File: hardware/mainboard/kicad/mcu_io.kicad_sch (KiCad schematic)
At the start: 37 parts, among them J2 Hirose DM3AT-SF-PEJM5, SW2 BOOT / RECOVERY, SW3 TL3340AF160QG, SW4 TL3340AF160QG, SW5 TL3340AF160QG, SW6 TL3340AF160QG, U1 ESP32-S3-WROOM-1-N16R8, U10 TLV3012BIDBVR, U5 BMI270, U9 TMUX1101DBVR

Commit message: R129: fix IC stencil apertures, pin-1 marking and native assembly classification
Verify six active IC pin maps and 97 native CPL placements. Preserve all 425 original pads, nets and 2639 tracks/vias; retain the 20 active intrinsic hole-clearance findings as fabrication gates. Add independent native KiCad checks and exact source-preservation guards.
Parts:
- U10: Assembly (none) -> FIT; MPN (none) -> TLV3012BIDBVR; Manufacturer (none) -> Texas Instruments
- U5: Assembly (none) -> FIT; MPN (none) -> BMI270; Manufacturer (none) -> Bosch Sensortec
- U9: Assembly (none) -> FIT; MPN (none) -> TMUX1101DBVR; Manufacturer (none) -> Texas Instruments
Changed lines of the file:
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@@
 		(property "Value" "BMI270" (at 188.26 132.86 0) (effects (font (size 0.88 0.88))))
 		(property "Footprint" "ENKU:BMI270_Bosch_LGA14" (at 175.26 149.86 0) (effects (font (size 0.88 0.88)) (hide yes)))
-		(property "Datasheet" "~" (at 175.26 149.86 0) (effects (font (size 0.88 0.88)) (hide yes)))
+		(property "Datasheet" "https://www.bosch-sensortec.com/media/boschsensortec/downloads/datasheets/bst-bmi270-ds000.pdf" (at 175.26 149.86 0) (effects (font (size 0.88 0.88)) (hide yes)))
 		(property "Description" "BMI270" (at 175.26 149.86 0) (effects (font (size 0.88 0.88)) (hide yes)))
 		(pin "1")
@@
 		(pin "14")
 		(instances (project "enku-mainboard-r0.1" (path "/10000000-0000-4000-8000-000000000001/74000000-0000-4000-8000-000000000182" (reference "U5") (unit 1))))
+		(property "Manufacturer" "Bosch Sensortec" (at 0 0 0) (effects (font (size .8 .8)) (hide yes)))
+		(property "MPN" "BMI270" (at 0 0 0) (effects (font (size .8 .8)) (hide yes)))
+		(property "Assembly" "FIT" (at 0 0 0) (effects (font (size .8 .8)) (hide yes)))
 	)
 	(global_label "GND" (shape input) (at 160.02 142.24 0) (effects (font (size 0.88 0.88)) (justify right bottom)))
@@
 (pin "5")
 (instances (project "enku-mainboard-r0.1" (path "/10000000-0000-4000-8000-000000000001/e4100000-0000-4000-8000-000000000001" (reference "U9") (unit 1))))
-)
+		(property "Manufacturer" "Texas Instruments" (at 0 0 0) (effects (font (size .8 .8)) (hide yes)))
+		(property "MPN" "TMUX1101DBVR" (at 0 0 0) (effects (font (size .8 .8)) (hide yes)))
+		(property "Assembly" "FIT" (at 0 0 0) (effects (font (size .8 .8)) (hide yes)))
+	)
 	(symbol (lib_id "ENKU:C") (at 367.03 167.64 0) (unit 1) (exclude_from_sim no) (in_bom yes) (on_board yes) (dnp no)
 (property "Reference" "C37" (at 362.03 151.64 0) (effects (font (size 0.88 0.88))))
@@
 (property "Value" "TLV3012BIDBVR" (at 330.2 210.82 0) (effects (font (size 0.88 0.88))))
 (property "Footprint" "ENKU:TLV3012B_DBV0006A" (at 330.2 210.82 0) (effects (font (size 0.88 0.88)) (hide yes)))
-(property "Datasheet" "https://www.ti.com/lit/gpn/TLV3012B" (at 330.2 210.82 0) (effects (font (size 0.88 0.88)) (hide yes)))
+(property "Datasheet" "https://www.ti.com/lit/ds/symlink/tlv3012b.pdf" (at 330.2 210.82 0) (effects (font (size 0.88 0.88)) (hide yes)))
 (property "Description" "TLV3012BIDBVR" (at 330.2 210.82 0) (effects (font (size 0.88 0.88)) (hide yes)))
 (pin "1")
@@
 (pin "5")
 (pin "6")
-(instances (project "enku-mainboard-r0.1" (path "/10000000-0000-4000-8000-000000000001/769db365-4ac6-4285-9803-94ba4cec03fc" (reference "U10") (unit 1)))))
+(instances (project "enku-mainboard-r0.1" (path "/10000000-0000-4000-8000-000000000001/769db365-4ac6-4285-9803-94ba4cec03fc" (reference "U10") (unit 1))))
+		(property "Manufacturer" "Texas Instruments" (at 0 0 0) (effects (font (size .8 .8)) (hide yes)))
+		(property "MPN" "TLV3012BIDBVR" (at 0 0 0) (effects (font (size .8 .8)) (hide yes)))
+		(property "Assembly" "FIT" (at 0 0 0) (effects (font (size .8 .8)) (hide yes)))
+	)
 (global_label "USB_VBUS_VALID" (shape input) (at 340.36 205.74 180) (effects (font (size 0.88 0.88)) (justify right bottom)))
 (global_label "GND" (shape input) (at 320.04 215.9 0) (effects (font (size 0.88 0.88)) (justify right bottom)))

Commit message: R130 BAT-REV3: PH2 battery and separate NTC; correct Laird lands and preserve R129
Implement the two-wire battery interface, retain all accepted copper identities, and restore the L2 land/via correction. Add native source/assembly/plot guards, supplier evidence and dimensional studies. Charging temperature, capacity/timer, complete mechanical fit and twenty hole findings remain HOLD; no fabrication or orders.
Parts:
- J2: Assembly (none) -> FIT; MPN (none) -> DM3AT-SF-PEJM5; Manufacturer (none) -> Hirose
- SW3, SW4, SW5, SW6: Assembly (none) -> FIT; MPN (none) -> TL3340AF160QG; Manufacturer (none) -> E-Switch
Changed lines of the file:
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@@
 		(property "Value" "TL3340AF160QG" (at 38.385 149.37 0) (effects (font (size 0.88 0.88))))
 		(property "Footprint" "ENKU:TL3340AF160QG_GEOMETRY_TRIAL" (at 32.385 166.37 0) (effects (font (size 0.88 0.88)) (hide yes)))
-		(property "Datasheet" "~" (at 32.385 166.37 0) (effects (font (size 0.88 0.88)) (hide yes)))
+		(property "Datasheet" "https://configured-product-images.s3.amazonaws.com/2D/specs/TL3340AF160QG.pdf" (at 32.385 166.37 0) (effects (font (size 0.88 0.88)) (hide yes)))
 		(property "Description" "BTN_L1" (at 32.385 166.37 0) (effects (font (size 0.88 0.88)) (hide yes)))
 		(pin "1")
 		(pin "3")
 		(instances (project "enku-mainboard-r0.1" (path "/10000000-0000-4000-8000-000000000001/74000000-0000-4000-8000-000000000110" (reference "SW3") (unit 1))))
+		(property "Manufacturer" "E-Switch" (at 0 0 0) (effects (font (size .8 .8)) (hide yes)))
+		(property "MPN" "TL3340AF160QG" (at 0 0 0) (effects (font (size .8 .8)) (hide yes)))
+		(property "Assembly" "FIT" (at 0 0 0) (effects (font (size .8 .8)) (hide yes)))
 	)
 	(global_label "BTN_L1" (shape input) (at 24.13 166.37 0) (effects (font (size 0.88 0.88)) (justify right bottom)))
@@
 		(property "Value" "TL3340AF160QG" (at 67.595 149.37 0) (effects (font (size 0.88 0.88))))
 		(property "Footprint" "ENKU:TL3340AF160QG_GEOMETRY_TRIAL" (at 61.595 166.37 0) (effects (font (size 0.88 0.88)) (hide yes)))
-		(property "Datasheet" "~" (at 61.595 166.37 0) (effects (font (size 0.88 0.88)) (hide yes)))
+		(property "Datasheet" "https://configured-product-images.s3.amazonaws.com/2D/specs/TL3340AF160QG.pdf" (at 61.595 166.37 0) (effects (font (size 0.88 0.88)) (hide yes)))
 		(property "Description" "BTN_L2" (at 61.595 166.37 0) (effects (font (size 0.88 0.88)) (hide yes)))
 		(pin "1")
 		(pin "3")
 		(instances (project "enku-mainboard-r0.1" (path "/10000000-0000-4000-8000-000000000001/74000000-0000-4000-8000-000000000115" (reference "SW4") (unit 1))))
+		(property "Manufacturer" "E-Switch" (at 0 0 0) (effects (font (size .8 .8)) (hide yes)))
+		(property "MPN" "TL3340AF160QG" (at 0 0 0) (effects (font (size .8 .8)) (hide yes)))
+		(property "Assembly" "FIT" (at 0 0 0) (effects (font (size .8 .8)) (hide yes)))
 	)
 	(global_label "BTN_L2" (shape input) (at 53.34 166.37 0) (effects (font (size 0.88 0.88)) (justify right bottom)))
@@
 		(property "Value" "TL3340AF160QG" (at 98.075 149.37 0) (effects (font (size 0.88 0.88))))
 		(property "Footprint" "ENKU:TL3340AF160QG_GEOMETRY_TRIAL" (at 92.075 166.37 0) (effects (font (size 0.88 0.88)) (hide yes)))
-		(property "Datasheet" "~" (at 92.075 166.37 0) (effects (font (size 0.88 0.88)) (hide yes)))
+		(property "Datasheet" "https://configured-product-images.s3.amazonaws.com/2D/specs/TL3340AF160QG.pdf" (at 92.075 166.37 0) (effects (font (size 0.88 0.88)) (hide yes)))
 		(property "Description" "BTN_R1" (at 92.075 166.37 0) (effects (font (size 0.88 0.88)) (hide yes)))
 		(pin "1")
 		(pin "3")
 		(instances (project "enku-mainboard-r0.1" (path "/10000000-0000-4000-8000-000000000001/74000000-0000-4000-8000-000000000120" (reference "SW5") (unit 1))))
+		(property "Manufacturer" "E-Switch" (at 0 0 0) (effects (font (size .8 .8)) (hide yes)))
+		(property "MPN" "TL3340AF160QG" (at 0 0 0) (effects (font (size .8 .8)) (hide yes)))
+		(property "Assembly" "FIT" (at 0 0 0) (effects (font (size .8 .8)) (hide yes)))
 	)
 	(global_label "BTN_R1" (shape input) (at 83.82 166.37 0) (effects (font (size 0.88 0.88)) (justify right bottom)))
@@
 		(property "Value" "TL3340AF160QG" (at 128.555 149.37 0) (effects (font (size 0.88 0.88))))
 		(property "Footprint" "ENKU:TL3340AF160QG_GEOMETRY_TRIAL" (at 122.555 166.37 0) (effects (font (size 0.88 0.88)) (hide yes)))
-		(property "Datasheet" "~" (at 122.555 166.37 0) (effects (font (size 0.88 0.88)) (hide yes)))
+		(property "Datasheet" "https://configured-product-images.s3.amazonaws.com/2D/specs/TL3340AF160QG.pdf" (at 122.555 166.37 0) (effects (font (size 0.88 0.88)) (hide yes)))
 		(property "Description" "BTN_R2" (at 122.555 166.37 0) (effects (font (size 0.88 0.88)) (hide yes)))
 		(pin "1")
 		(pin "3")
 		(instances (project "enku-mainboard-r0.1" (path "/10000000-0000-4000-8000-000000000001/74000000-0000-4000-8000-000000000125" (reference "SW6") (unit 1))))
+		(property "Manufacturer" "E-Switch" (at 0 0 0) (effects (font (size .8 .8)) (hide yes)))
+		(property "MPN" "TL3340AF160QG" (at 0 0 0) (effects (font (size .8 .8)) (hide yes)))
+		(property "Assembly" "FIT" (at 0 0 0) (effects (font (size .8 .8)) (hide yes)))
 	)
 	(global_label "BTN_R2" (shape input) (at 114.3 166.37 0) (effects (font (size 0.88 0.88)) (justify right bottom)))
@@
 		(property "Value" "Hirose DM3AT-SF-PEJM5" (at 185.625 41.42 0) (effects (font (size 0.88 0.88))))
 		(property "Footprint" "ENKU:MICROSD_DM3AT_ENKU" (at 174.625 58.42 0) (effects (font (size 0.88 0.88)) (hide yes)))
-		(property "Datasheet" "~" (at 174.625 58.42 0) (effects (font (size 0.88 0.88)) (hide yes)))
+		(property "Datasheet" "https://www.hirose.com/en/product/p/CL0609-0031-0-00" (at 174.625 58.42 0) (effects (font (size 0.88 0.88)) (hide yes)))
 		(property "Description" "Hirose DM3AT-SF-PEJM5" (at 174.625 58.42 0) (effects (font (size 0.88 0.88)) (hide yes)))
 		(pin "1")
@@
 		(pin "8")
 		(instances (project "enku-mainboard-r0.1" (path "/10000000-0000-4000-8000-000000000001/74000000-0000-4000-8000-000000000130" (reference "J2") (unit 1))))
+		(property "Manufacturer" "Hirose" (at 0 0 0) (effects (font (size .8 .8)) (hide yes)))
+		(property "MPN" "DM3AT-SF-PEJM5" (at 0 0 0) (effects (font (size .8 .8)) (hide yes)))
+		(property "Assembly" "FIT" (at 0 0 0) (effects (font (size .8 .8)) (hide yes)))
 	)
 	(global_label "SD_CS_CARD" (shape input) (at 161.29 57.15 0) (effects (font (size 0.88 0.88)) (justify right bottom)))

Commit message: R134 working checkpoint: real USB4215 replacement and GPIO charger control; ten routes pending, NO FAB
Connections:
- net CHG_CE_CMD: now reaches U1.31 (GPIO38)
- net CHG_EN2_CMD: now reaches U1.38 (GPIO2)
- net CHG_EN1_CMD: now reaches U1.9 (GPIO16)
- no-connect marks 24 -> 21
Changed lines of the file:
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@@
 	(global_label "BTN_R2" (shape input) (at 60.96 73.66 0) (effects (font (size 0.88 0.88)) (justify right bottom)))
 	(global_label "CHG_STAT1" (shape input) (at 60.96 76.2 0) (effects (font (size 0.88 0.88)) (justify right bottom)))
-	(no_connect (at 60.96 78.74))
 	(global_label "USB_VBUS_VALID" (shape input) (at 60.96 81.28 0) (effects (font (size 0.88 0.88)) (justify right bottom)))
 	(global_label "IMU_INT1" (shape input) (at 60.96 83.82 0) (effects (font (size 0.88 0.88)) (justify right bottom)))
@@
 	(global_label "EPD_BUSY" (shape output) (at 104.14 69.85 180) (effects (font (size 0.88 0.88)) (justify right bottom)))
 	(global_label "BOOT" (shape output) (at 104.14 74.93 180) (effects (font (size 0.88 0.88)) (justify right bottom)))
-	(no_connect (at 104.14 85.09))
 	(no_connect (at 104.14 87.63))
 	(no_connect (at 104.14 90.17))
@@
 	(global_label "UART_RX" (shape output) (at 104.14 97.79 180) (effects (font (size 0.88 0.88)) (justify right bottom)))
 	(global_label "UART_TX" (shape output) (at 104.14 100.33 180) (effects (font (size 0.88 0.88)) (justify right bottom)))
-	(no_connect (at 104.14 102.87))
 	(global_label "BAT_ADC" (shape output) (at 104.14 105.41 180) (effects (font (size 0.88 0.88)) (justify right bottom)))
 	(no_connect (at 60.96 93.98))
@@
 	(no_connect (at 92.71 173.99))
 	(no_connect (at 123.19 173.99))
+(global_label "CHG_EN1_CMD" (shape input) (at 60.960000 78.740000 0) (effects (font (size .88 .88)) (justify right bottom)))
+(global_label "CHG_EN2_CMD" (shape input) (at 104.140000 102.870000 180) (effects (font (size .88 .88)) (justify left bottom)))
+(global_label "CHG_CE_CMD" (shape input) (at 104.140000 85.090000 180) (effects (font (size .88 .88)) (justify left bottom)))
 )

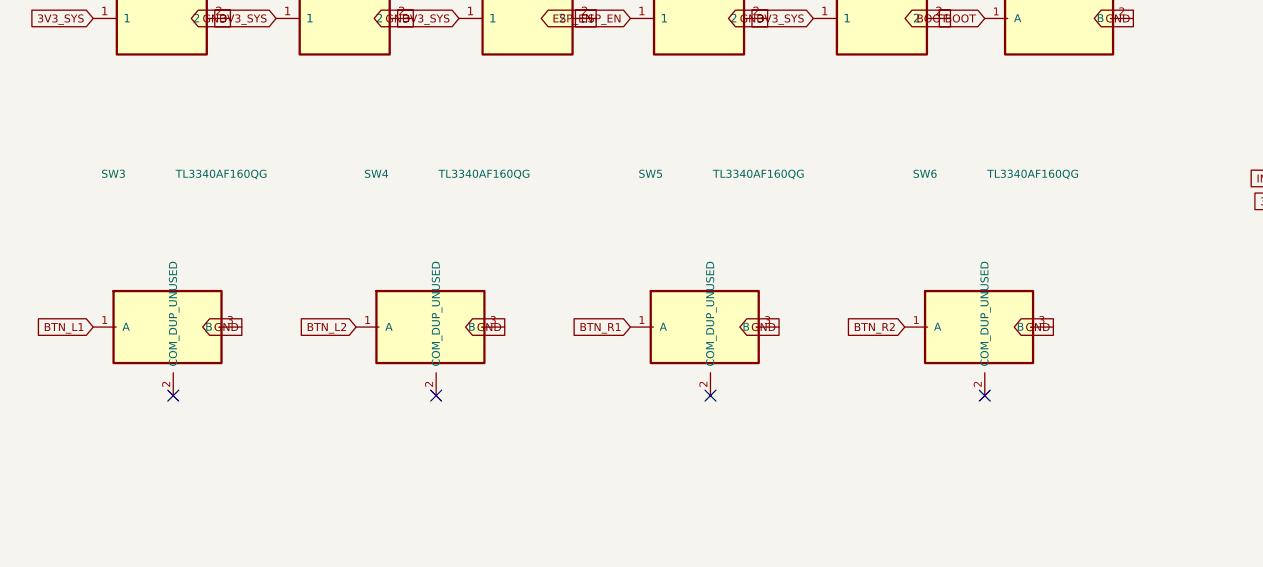
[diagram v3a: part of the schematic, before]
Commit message: R135 native DRC/ERC/parity zero after genuine no-boss switches and TS bias correction; independent audits pending, NO FAB
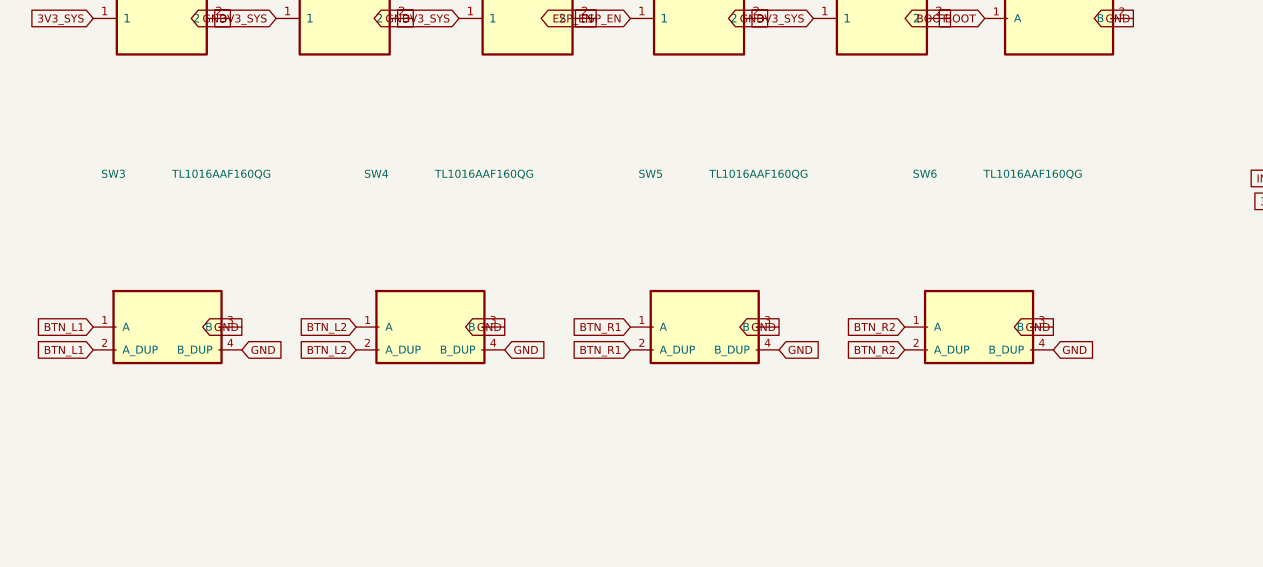
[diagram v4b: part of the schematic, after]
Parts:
- SW3, SW4, SW5, SW6: value TL3340AF160QG -> TL1016AAF160QG; footprint ENKU:TL3340AF160QG_GEOMETRY_TRIAL -> ENKU:TL1016AAF160QG_ESWITCH_P520001; symbol ENKU:TL3340_3PIN -> ENKU:TL1016_AA_4PIN; MPN TL3340AF160QG -> TL1016AAF160QG
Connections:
- net BTN_L1: now also SW3.2 (A_DUP)
- net BTN_L2: now also SW4.2 (A_DUP)
- net BTN_R1: now also SW5.2 (A_DUP)
- net BTN_R2: now also SW6.2 (A_DUP)
- net GND: now also SW3.4 (B_DUP), SW4.4 (B_DUP), SW5.4 (B_DUP), SW6.4 (B_DUP)
- no-connect marks 21 -> 17
